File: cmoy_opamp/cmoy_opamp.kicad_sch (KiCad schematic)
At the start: 33 parts, among them J1 AudioJack3, J2 AudioJack3, SW1 SPST, U1 MC33178, U2 LMH6642, U3 LMH6642, U4 LMH6642

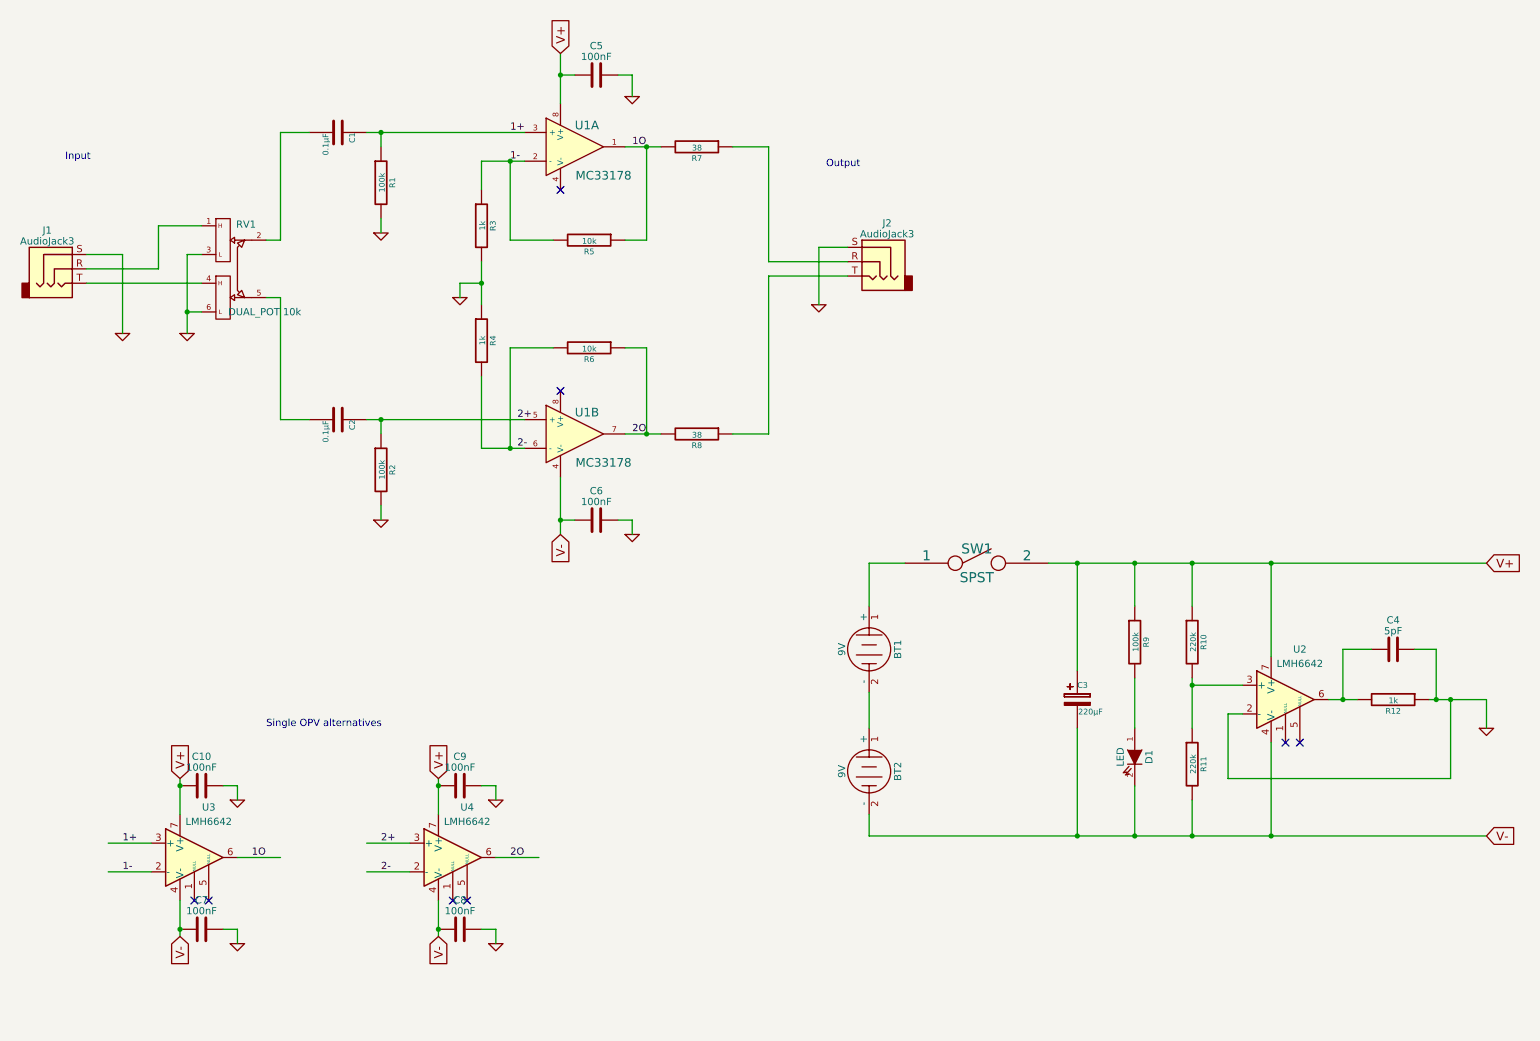
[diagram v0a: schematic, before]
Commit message: dual footprint, THT and SMD, first layouting
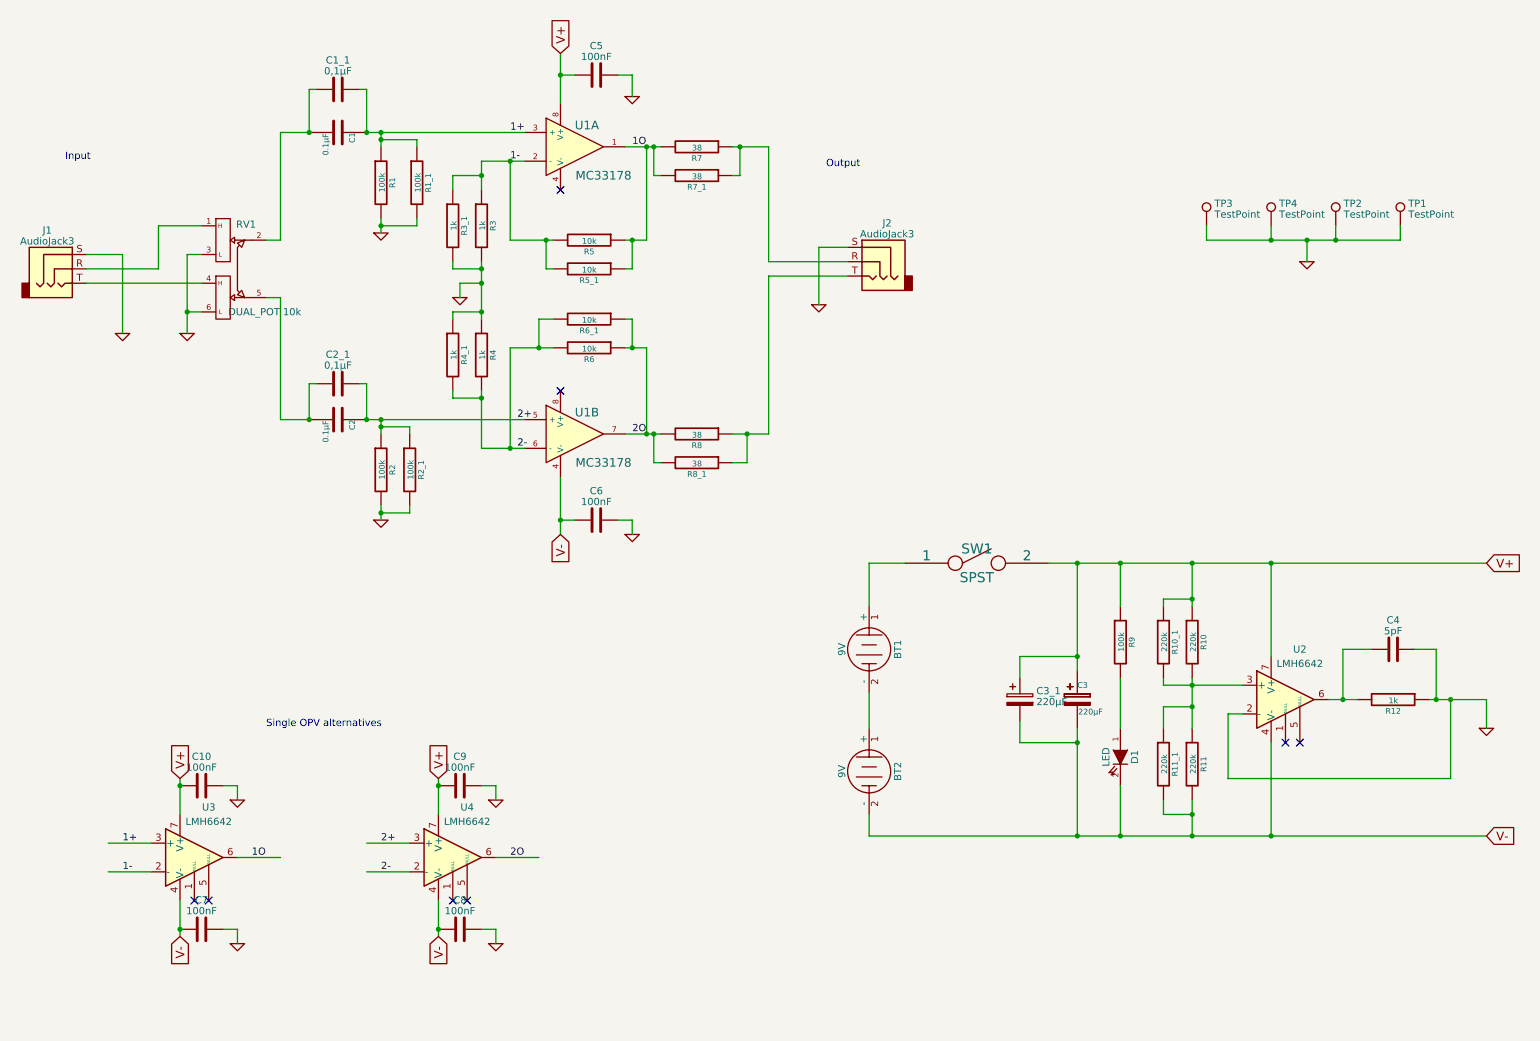
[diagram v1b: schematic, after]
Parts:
- added C1_1, C2_1: 0,1µF, Capacitor_THT:C_Rect_L7.0mm_W6.0mm_P5.00mm, symbol Device:C
- added C3_1: 220µF, Capacitor_THT:CP_Radial_D10.0mm_P3.50mm, symbol Device:C_Polarized
- added R10_1, R11_1: 220k, Resistor_THT:R_Axial_DIN0204_L3.6mm_D1.6mm_P7.62mm_Horizontal, symbol d2k2_cmoy-rescue:R
- added R1_1, R2_1: 100k, Resistor_THT:R_Axial_DIN0204_L3.6mm_D1.6mm_P7.62mm_Horizontal, symbol d2k2_cmoy-rescue:R
- added R3_1, R4_1: 1k, Resistor_THT:R_Axial_DIN0204_L3.6mm_D1.6mm_P7.62mm_Horizontal, symbol d2k2_cmoy-rescue:R
- added R5_1, R6_1: 10k, Resistor_THT:R_Axial_DIN0204_L3.6mm_D1.6mm_P7.62mm_Horizontal, symbol d2k2_cmoy-rescue:R
- added R7_1, R8_1: 38, Resistor_THT:R_Axial_DIN0204_L3.6mm_D1.6mm_P7.62mm_Horizontal, symbol d2k2_cmoy-rescue:R
- added TP1, TP2, TP3, TP4: TestPoint, Connector_PinSocket_2.54mm:PinSocket_1x01_P2.54mm_Vertical, symbol Connector:TestPoint
- R1, R10, R11, R12, R2, R3, R4, R5, R6, R7, R8, R9: footprint Resistor_SMD:R_0805_2012Metric -> Resistor_SMD:R_1206_3216Metric
- U2: footprint Package_SO:SOIC-8-N7_3.9x4.9mm_P1.27mm -> Package_SO:SOIC-8_3.9x4.9mm_P1.27mm
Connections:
- net 1+: now also C1_1.2, R1_1.1
- net 1-: now also R3_1.1, R5_1.2
- net 1O: now also R5_1.1, R7_1.2
- net 2+: now also C2_1.2, R2_1.1
- net 2-: now also R4_1.2, R6_1.2
- net 2O: now also R6_1.1, R8_1.2
- net GND: now also R1_1.2, R2_1.2, R3_1.2, R4_1.1, TP1.1, TP2.1, TP3.1, TP4.1
- net V+: now also C3_1.1, R10_1.1
- net V-: now also C3_1.2, R11_1.2
- net at C1.2, RV1.2: now also C1_1.1
- net at C2.2, RV1.5: now also C2_1.1
- net at J2.R, R7.1: now also R7_1.1
- net at J2.T, R8.1: now also R8_1.1
- net at R10.2, R11.1, U2.3 (+): now also R10_1.2, R11_1.1
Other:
- moved on the sheet: D1, R4, R9

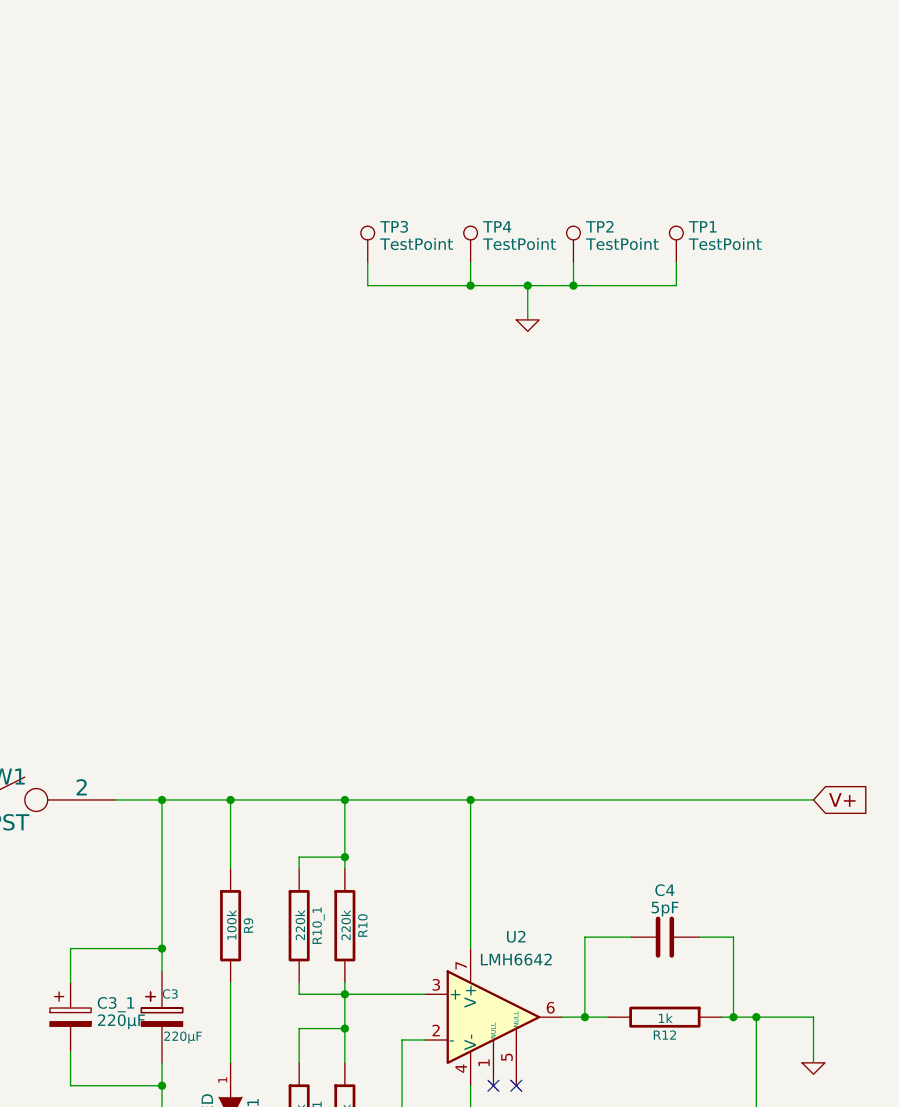
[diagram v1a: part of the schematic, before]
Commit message: PCB Layout complete
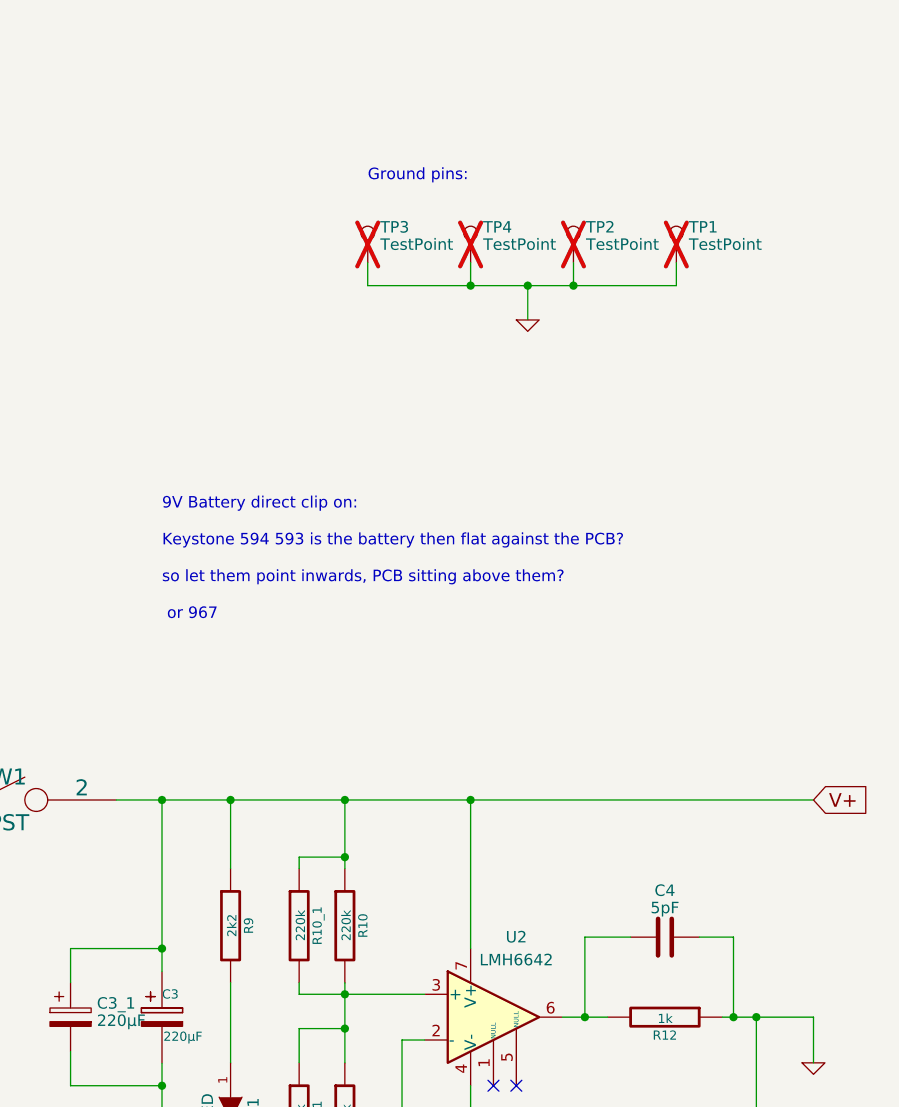
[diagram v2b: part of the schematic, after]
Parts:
- R9: value 100k -> 2k2
- TP1, TP2, TP3, TP4: now not fitted; now left out of the parts list
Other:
- note added: "9V Battery direct clip on: Keystone 594 593 is the battery then flat against the PCB? so let them point inwards, PCB sitting above them? or 967"
- note added: "Ground pins:"
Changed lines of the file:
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@@
     (stroke (width 0) (type default))
+  )
+  (text "9V Battery direct clip on:\n\nKeystone 594 593 is the battery then flat against the PCB?\n\nso let them point inwards, PCB sitting above them? \n\n or 967\n\n"
+    (at 200.66 92.71 0)
+    (effects (font (size 1.27 1.27)) (justify left bottom))
   )
   (text "Input" (at 21.59 39.37 0)
@@
   )
   (text "Single OPV alternatives" (at 57.15 139.7 0)
+    (effects (font (size 1.27 1.27)) (justify left bottom))
+  )
+  (text "Ground pins:" (at 223.52 41.91 0)
     (effects (font (size 1.27 1.27)) (justify left bottom))
   )
@@
       (effects (font (size 1.016 1.016)))
     )
-    (property "Value" "100k" (at 208.4578 124.4346 90)
+    (property "Value" "2k2" (at 208.4578 124.4346 90)
       (effects (font (size 1.016 1.016)))
     )
@@
   )
   (symbol (lib_id "Connector:TestPoint") (at 257.81 50.8 0) (unit 1)
-    (in_bom yes) (on_board yes) (dnp no) (fields_autoplaced)
+    (in_bom no) (on_board yes) (dnp yes) (fields_autoplaced)
     (property "Reference" "TP1" (at 259.207 46.8543 0)
       (effects (font (size 1.27 1.27)) (justify left))
@@
   )
   (symbol (lib_id "Connector:TestPoint") (at 246.38 50.8 0) (unit 1)
-    (in_bom yes) (on_board yes) (dnp no) (fields_autoplaced)
+    (in_bom no) (on_board yes) (dnp yes) (fields_autoplaced)
     (property "Reference" "TP2" (at 247.777 46.8543 0)
       (effects (font (size 1.27 1.27)) (justify left))
@@
   )
   (symbol (lib_id "Connector:TestPoint") (at 234.95 50.8 0) (unit 1)
-    (in_bom yes) (on_board yes) (dnp no) (fields_autoplaced)
+    (in_bom no) (on_board yes) (dnp yes) (fields_autoplaced)
     (property "Reference" "TP4" (at 236.347 46.8543 0)
       (effects (font (size 1.27 1.27)) (justify left))
@@
   )
   (symbol (lib_id "Connector:TestPoint") (at 223.52 50.8 0) (unit 1)
-    (in_bom yes) (on_board yes) (dnp no) (fields_autoplaced)
+    (in_bom no) (on_board yes) (dnp yes) (fields_autoplaced)
     (property "Reference" "TP3" (at 224.917 46.8543 0)
       (effects (font (size 1.27 1.27)) (justify left))

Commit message: PCB art added
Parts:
- added R12_1: 1k, Resistor_THT:R_Axial_DIN0204_L3.6mm_D1.6mm_P7.62mm_Horizontal, symbol d2k2_cmoy-rescue:R
- C1_1, C2_1: Part (none) -> BFC237011105
- C2: Part (none) -> MKT1813410405
- J1, J2: Part (none) -> SJ1-3523N
- RV1: Name RK09712200HA -> (none); Part (none) -> RK09712200HA
- SW1: Part (none) -> OS102011MA1QN1
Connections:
- net GND: now also R12_1.1
- net at C4.1, R12.2, U2.6: now also R12_1.2
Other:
- note added: "ToDo: Add Partnumbers"
- note removed: "9V Battery direct clip on: Keystone 594 593 is the battery then flat against the PCB? so let them point inwards, PCB sitting above them? or 967"
- moved on the sheet: C10, C7, C8, C9, TP1, TP2, TP3, TP4, U3, U4

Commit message: Documentation files updated
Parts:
- C1: Part (none) -> MKT1813410405
- U2: Part (none) -> LMH6642MA
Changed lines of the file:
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@@
       (effects (font (size 0.762 0.762)) hide)
     )
-    (property "Datasheet" "MKT1813410405" (at 69.85 34.29 0)
+    (property "Datasheet" "" (at 69.85 34.29 0)
       (effects (font (size 1.524 1.524)) hide)
+    )
+    (property "Part" "MKT1813410405" (at 69.85 34.29 0)
+      (effects (font (size 1.27 1.27)) hide)
     )
     (pin "1")
@@
       (effects (font (size 1.27 1.27)) hide)
     )
+    (property "Part" "LMH6642MA" (at 237.49 134.62 0)
+      (effects (font (size 1.27 1.27)) hide)
+    )
